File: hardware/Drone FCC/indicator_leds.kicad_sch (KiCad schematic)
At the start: 48 parts, among them Q1101 2N7002, Q1102 2N7002, Q1103 2N7002, Q1104 2N7002, Q1105 2N7002, Q1106 2N7002, Q1107 2N7002, Q1108 2N7002, SW1101 SW Proposito General, SW1102 SW Proposito General

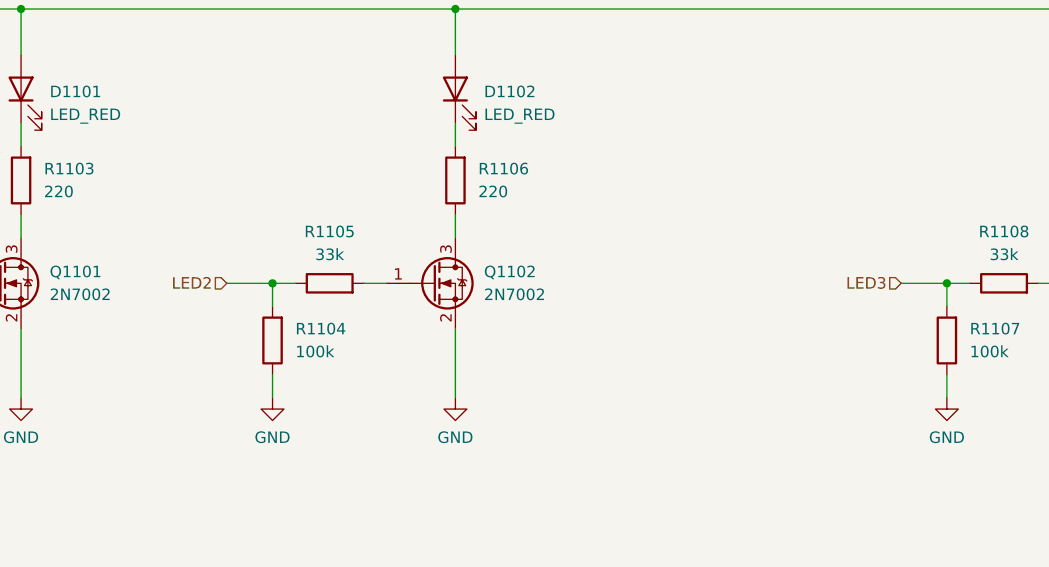
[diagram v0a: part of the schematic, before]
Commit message: re routed everything with newer dimensions
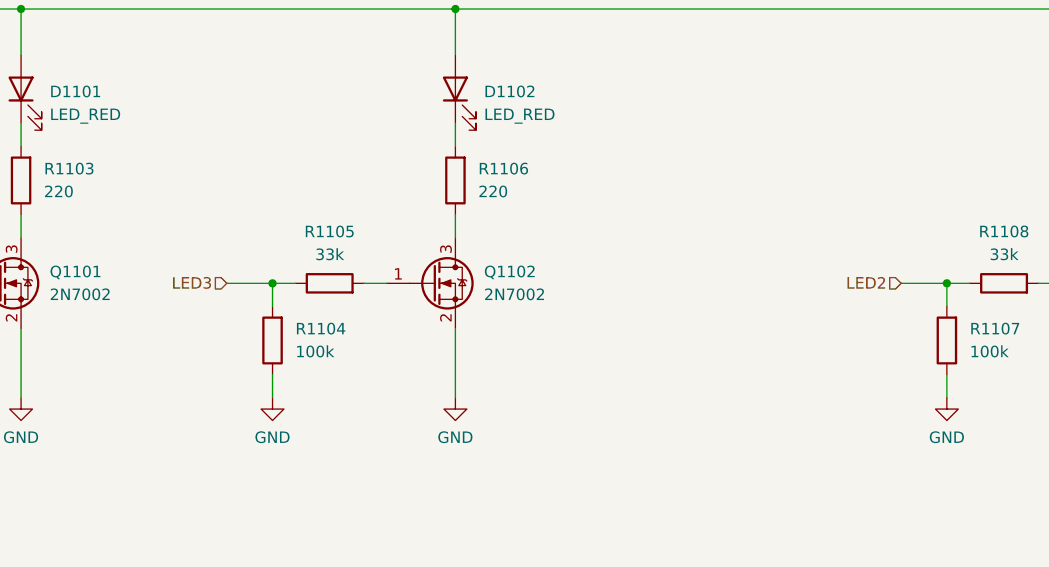
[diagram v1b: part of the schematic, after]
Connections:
- net LED2: now also R1107.2, R1108.1; no longer R1104.2, R1105.1
- net LED3: now also R1104.2, R1105.1; no longer R1107.2, R1108.1
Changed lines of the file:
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@@
     (effects (font (size 1.27 1.27)) (justify right))
   )
-  (hierarchical_label "LED3" (shape input) (at 167.64 47.625 180)
+  (hierarchical_label "LED3" (shape input) (at 92.71 47.625 180)
     (effects (font (size 1.27 1.27)) (justify right))
   )
@@
     (effects (font (size 1.27 1.27)) (justify right))
   )
-  (hierarchical_label "LED2" (shape input) (at 92.71 47.625 180)
+  (hierarchical_label "LED2" (shape input) (at 167.64 47.625 180)
     (effects (font (size 1.27 1.27)) (justify right))
   )

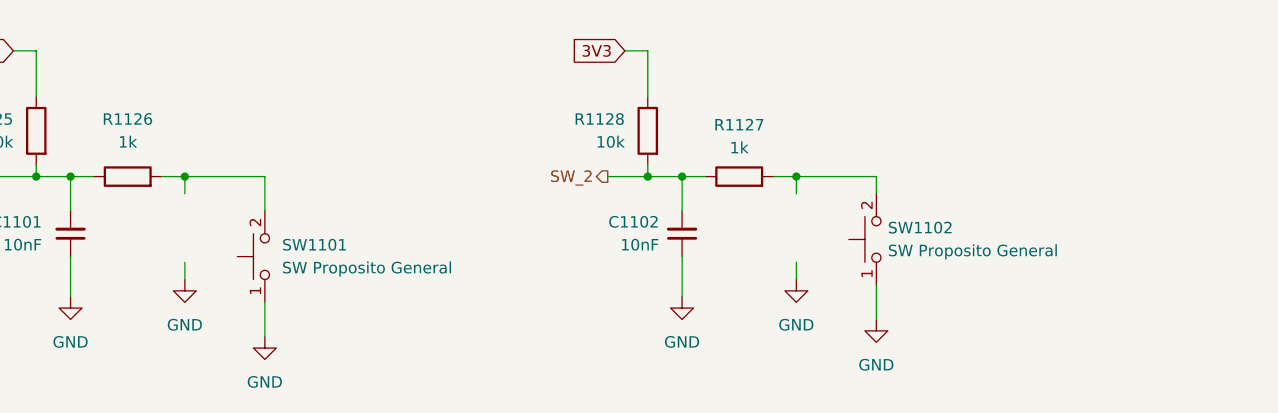
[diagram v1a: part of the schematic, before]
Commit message: tidying up the schematic
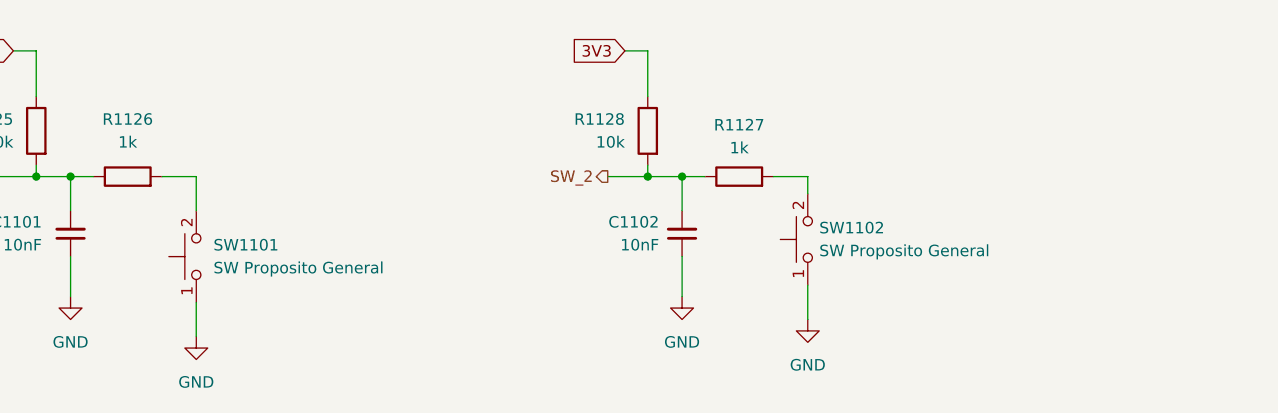
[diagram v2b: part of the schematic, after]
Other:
- moved on the sheet: SW1101, SW1102
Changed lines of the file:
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@@
   (junction (at 29.845 167.64) (diameter 0) (color 0 0 0 0)
   )
-  (junction (at 110.49 167.64) (diameter 0) (color 0 0 0 0)
-  )
   (junction (at 93.98 167.64) (diameter 0) (color 0 0 0 0)
   )
-  (junction (at 42.545 167.64) (diameter 0) (color 0 0 0 0)
-  )
   (junction (at 220.98 47.625) (diameter 0) (color 0 0 0 0)
   )
@@
     (stroke (width 0) (type default) (color 0 0 0 0))
   )
-  (wire (pts (xy 51.435 167.64) (xy 51.435 171.45))
+  (wire (pts (xy 43.815 167.64) (xy 43.815 171.45))
+    (stroke (width 0) (type default) (color 0 0 0 0))
+  )
+  (wire (pts (xy 40.005 167.64) (xy 43.815 167.64))
     (stroke (width 0) (type default) (color 0 0 0 0))
   )
@@
     (stroke (width 0) (type default) (color 0 0 0 0))
   )
-  (wire (pts (xy 119.38 167.64) (xy 119.38 169.545))
+  (wire (pts (xy 111.76 167.64) (xy 111.76 169.545))
     (stroke (width 0) (type default) (color 0 0 0 0))
   )
@@
     (stroke (width 0) (type default) (color 0 0 0 0))
   )
-  (wire (pts (xy 110.49 177.165) (xy 110.49 179.07))
-    (stroke (width 0) (type default) (color 0 0 0 0))
-  )
   (wire (pts (xy 106.045 127.635) (xy 108.585 127.635))
     (stroke (width 0) (type default) (color 0 0 0 0))
@@
     (stroke (width 0) (type default) (color 0 0 0 0))
   )
-  (wire (pts (xy 110.49 167.64) (xy 119.38 167.64))
+  (wire (pts (xy 107.95 167.64) (xy 111.76 167.64))
     (stroke (width 0) (type default) (color 0 0 0 0))
   )
@@
     (stroke (width 0) (type default) (color 0 0 0 0))
   )
-  (wire (pts (xy 40.005 167.64) (xy 42.545 167.64))
-    (stroke (width 0) (type default) (color 0 0 0 0))
-  )
   (wire (pts (xy 116.205 132.715) (xy 116.205 140.335))
     (stroke (width 0) (type default) (color 0 0 0 0))
@@
     (stroke (width 0) (type default) (color 0 0 0 0))
   )
-  (wire (pts (xy 119.38 179.705) (xy 119.38 183.515))
+  (wire (pts (xy 111.76 179.705) (xy 111.76 183.515))
     (stroke (width 0) (type default) (color 0 0 0 0))
   )
@@
     (stroke (width 0) (type default) (color 0 0 0 0))
   )
-  (wire (pts (xy 42.545 177.165) (xy 42.545 179.07))
-    (stroke (width 0) (type default) (color 0 0 0 0))
-  )
   (wire (pts (xy 97.79 176.53) (xy 97.79 180.975))
     (stroke (width 0) (type default) (color 0 0 0 0))
@@
     (stroke (width 0) (type default) (color 0 0 0 0))
   )
-  (wire (pts (xy 51.435 181.61) (xy 51.435 185.42))
+  (wire (pts (xy 43.815 181.61) (xy 43.815 185.42))
     (stroke (width 0) (type default) (color 0 0 0 0))
   )
@@
     (stroke (width 0) (type default) (color 0 0 0 0))
   )
-  (wire (pts (xy 42.545 167.64) (xy 42.545 169.545))
-    (stroke (width 0) (type default) (color 0 0 0 0))
-  )
   (wire (pts (xy 231.14 127.635) (xy 233.68 127.635))
     (stroke (width 0) (type default) (color 0 0 0 0))
@@
     (stroke (width 0) (type default) (color 0 0 0 0))
   )
-  (wire (pts (xy 110.49 167.64) (xy 110.49 169.545))
-    (stroke (width 0) (type default) (color 0 0 0 0))
-  )
   (wire (pts (xy 69.85 40.005) (xy 69.85 42.545))
     (stroke (width 0) (type default) (color 0 0 0 0))
   )
-  (wire (pts (xy 42.545 167.64) (xy 51.435 167.64))
-    (stroke (width 0) (type default) (color 0 0 0 0))
-  )
   (wire (pts (xy 50.165 127.635) (xy 47.625 127.635))
     (stroke (width 0) (type default) (color 0 0 0 0))
@@
   )
   (wire (pts (xy 116.205 97.155) (xy 193.04 97.155))
-    (stroke (width 0) (type default) (color 0 0 0 0))
-  )
-  (wire (pts (xy 107.95 167.64) (xy 110.49 167.64))
     (stroke (width 0) (type default) (color 0 0 0 0))
   )
@@
     (pin "1")
   )
-  (symbol (lib_id "power:GND") (at 119.38 183.515 0) (unit 1)
-    (in_bom yes) (on_board yes) (fields_autoplaced)
-    (property "Reference" "#PWR0165" (id 0) (at 119.38 189.865 0)
-      (effects (font (size 1.27 1.27)) hide)
-    )
-    (property "Value" "GND" (id 1) (at 119.38 188.595 0))
-    (property "Footprint" "" (id 2) (at 119.38 183.515 0)
-      (effects (font (size 1.27 1.27)) hide)
-    )
-    (property "Datasheet" "" (id 3) (at 119.38 183.515 0)
+  (symbol (lib_id "power:GND") (at 111.76 183.515 0) (unit 1)
+    (in_bom yes) (on_board yes) (fields_autoplaced)
+    (property "Reference" "#PWR0165" (id 0) (at 111.76 189.865 0)
+      (effects (font (size 1.27 1.27)) hide)
+    )
+    (property "Value" "GND" (id 1) (at 111.76 188.595 0))
+    (property "Footprint" "" (id 2) (at 111.76 183.515 0)
+      (effects (font (size 1.27 1.27)) hide)
+    )
+    (property "Datasheet" "" (id 3) (at 111.76 183.515 0)
       (effects (font (size 1.27 1.27)) hide)
     )
@@
     (pin "1")
   )
-  (symbol (lib_id "power:GND") (at 42.545 179.07 0) (unit 1)
-    (in_bom yes) (on_board yes) (fields_autoplaced)
-    (property "Reference" "#PWR0215" (id 0) (at 42.545 185.42 0)
-      (effects (font (size 1.27 1.27)) hide)
-    )
-    (property "Value" "GND" (id 1) (at 42.545 184.15 0))
-    (property "Footprint" "" (id 2) (at 42.545 179.07 0)
-      (effects (font (size 1.27 1.27)) hide)
-    )
-    (property "Datasheet" "" (id 3) (at 42.545 179.07 0)
-      (effects (font (size 1.27 1.27)) hide)
-    )
-    (pin "1")
-  )
   (symbol (lib_id "Device:LED") (at 67.945 106.045 90) (unit 1)
     (in_bom yes) (on_board yes) (fields_autoplaced)
@@
     (pin "3")
   )
-  (symbol (lib_id "power:GND") (at 110.49 179.07 0) (unit 1)
-    (in_bom yes) (on_board yes) (fields_autoplaced)
-    (property "Reference" "#PWR0217" (id 0) (at 110.49 185.42 0)
-      (effects (font (size 1.27 1.27)) hide)
-    )
-    (property "Value" "GND" (id 1) (at 110.49 184.15 0))
-    (property "Footprint" "" (id 2) (at 110.49 179.07 0)
-      (effects (font (size 1.27 1.27)) hide)
-    )
-    (property "Datasheet" "" (id 3) (at 110.49 179.07 0)
-      (effects (font (size 1.27 1.27)) hide)
-    )
-    (pin "1")
-  )
   (symbol (lib_id "Device:R") (at 220.98 133.985 180) (unit 1)
     (in_bom yes) (on_board yes) (fields_autoplaced)
@@
     (pin "2")
   )
-  (symbol (lib_id "434121043816:SW_SPST") (at 119.38 174.625 90) (unit 1)
+  (symbol (lib_id "434121043816:SW_SPST") (at 111.76 174.625 90) (unit 1)
     (in_bom yes) (on_board yes)
-    (property "Reference" "SW1102" (id 0) (at 120.65 173.3549 90)
-      (effects (font (size 1.27 1.27)) (justify right))
-    )
-    (property "Value" "SW Proposito General" (id 1) (at 120.65 175.8949 90)
-      (effects (font (size 1.27 1.27)) (justify right))
-    )
-    (property "Footprint" "434121043816:434121043816" (id 2) (at 119.38 174.625 0)
-      (effects (font (size 1.27 1.27)) hide)
-    )
-    (property "Datasheet" "~" (id 3) (at 119.38 174.625 0)
+    (property "Reference" "SW1102" (id 0) (at 113.03 173.3549 90)
+      (effects (font (size 1.27 1.27)) (justify right))
+    )
+    (property "Value" "SW Proposito General" (id 1) (at 113.03 175.8949 90)
+      (effects (font (size 1.27 1.27)) (justify right))
+    )
+    (property "Footprint" "434121043816:434121043816" (id 2) (at 111.76 174.625 0)
+      (effects (font (size 1.27 1.27)) hide)
+    )
+    (property "Datasheet" "~" (id 3) (at 111.76 174.625 0)
       (effects (font (size 1.27 1.27)) hide)
     )
@@
     (pin "1")
   )
-  (symbol (lib_id "434121043816:SW_SPST") (at 51.435 176.53 90) (unit 1)
-    (in_bom yes) (on_board yes) (fields_autoplaced)
-    (property "Reference" "SW1101" (id 0) (at 53.34 175.2599 90)
-      (effects (font (size 1.27 1.27)) (justify right))
-    )
-    (property "Value" "SW Proposito General" (id 1) (at 53.34 177.7999 90)
-      (effects (font (size 1.27 1.27)) (justify right))
-    )
-    (property "Footprint" "434121043816:434121043816" (id 2) (at 51.435 176.53 0)
-      (effects (font (size 1.27 1.27)) hide)
-    )
-    (property "Datasheet" "~" (id 3) (at 51.435 176.53 0)
+  (symbol (lib_id "434121043816:SW_SPST") (at 43.815 176.53 90) (unit 1)
+    (in_bom yes) (on_board yes) (fields_autoplaced)
+    (property "Reference" "SW1101" (id 0) (at 45.72 175.2599 90)
+      (effects (font (size 1.27 1.27)) (justify right))
+    )
+    (property "Value" "SW Proposito General" (id 1) (at 45.72 177.7999 90)
+      (effects (font (size 1.27 1.27)) (justify right))
+    )
+    (property "Footprint" "434121043816:434121043816" (id 2) (at 43.815 176.53 0)
+      (effects (font (size 1.27 1.27)) hide)
+    )
+    (property "Datasheet" "~" (id 3) (at 43.815 176.53 0)
       (effects (font (size 1.27 1.27)) hide)
     )
@@
     (pin "1")
   )
-  (symbol (lib_id "power:GND") (at 51.435 185.42 0) (unit 1)
-    (in_bom yes) (on_board yes) (fields_autoplaced)
-    (property "Reference" "#PWR0214" (id 0) (at 51.435 191.77 0)
-      (effects (font (size 1.27 1.27)) hide)
-    )
-    (property "Value" "GND" (id 1) (at 51.435 190.5 0))
-    (property "Footprint" "" (id 2) (at 51.435 185.42 0)
-      (effects (font (size 1.27 1.27)) hide)
-    )
-    (property "Datasheet" "" (id 3) (at 51.435 185.42 0)
-      (effects (font (size 1.27 1.27)) hide)
-    )
+  (symbol (lib_id "power:GND") (at 43.815 185.42 0) (unit 1)
+    (in_bom yes) (on_board yes) (fields_autoplaced)
+    (property "Reference" "#PWR0214" (id 0) (at 43.815 191.77 0)
+      (effects (font (size 1.27 1.27)) hide)
+    )
+    (property "Value" "GND" (id 1) (at 43.815 190.5 0))
+    (property "Footprint" "" (id 2) (at 43.815 185.42 0)
+      (effects (font (size 1.27 1.27)) hide)
+    )
+    (property "Datasheet" "" (id 3) (at 43.815 185.42 0)
+      (effects (font (size 1.27 1.27)) hide)
+    )

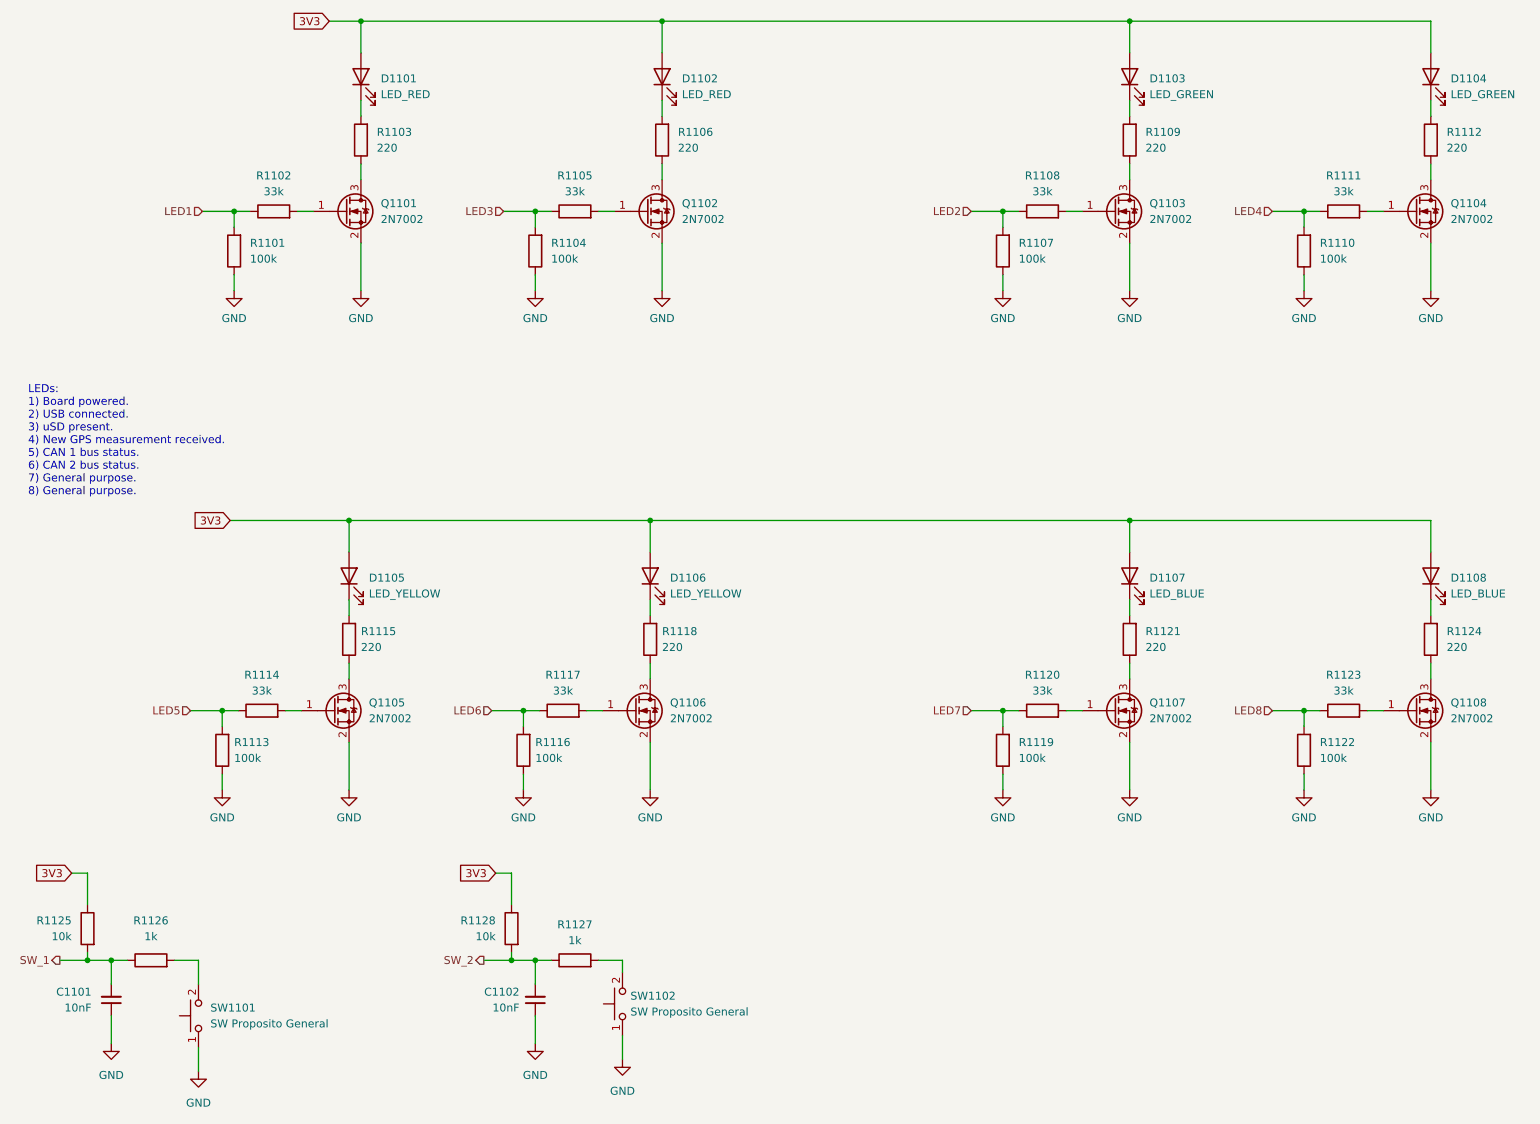
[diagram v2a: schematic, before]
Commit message: re enumeation of componentes
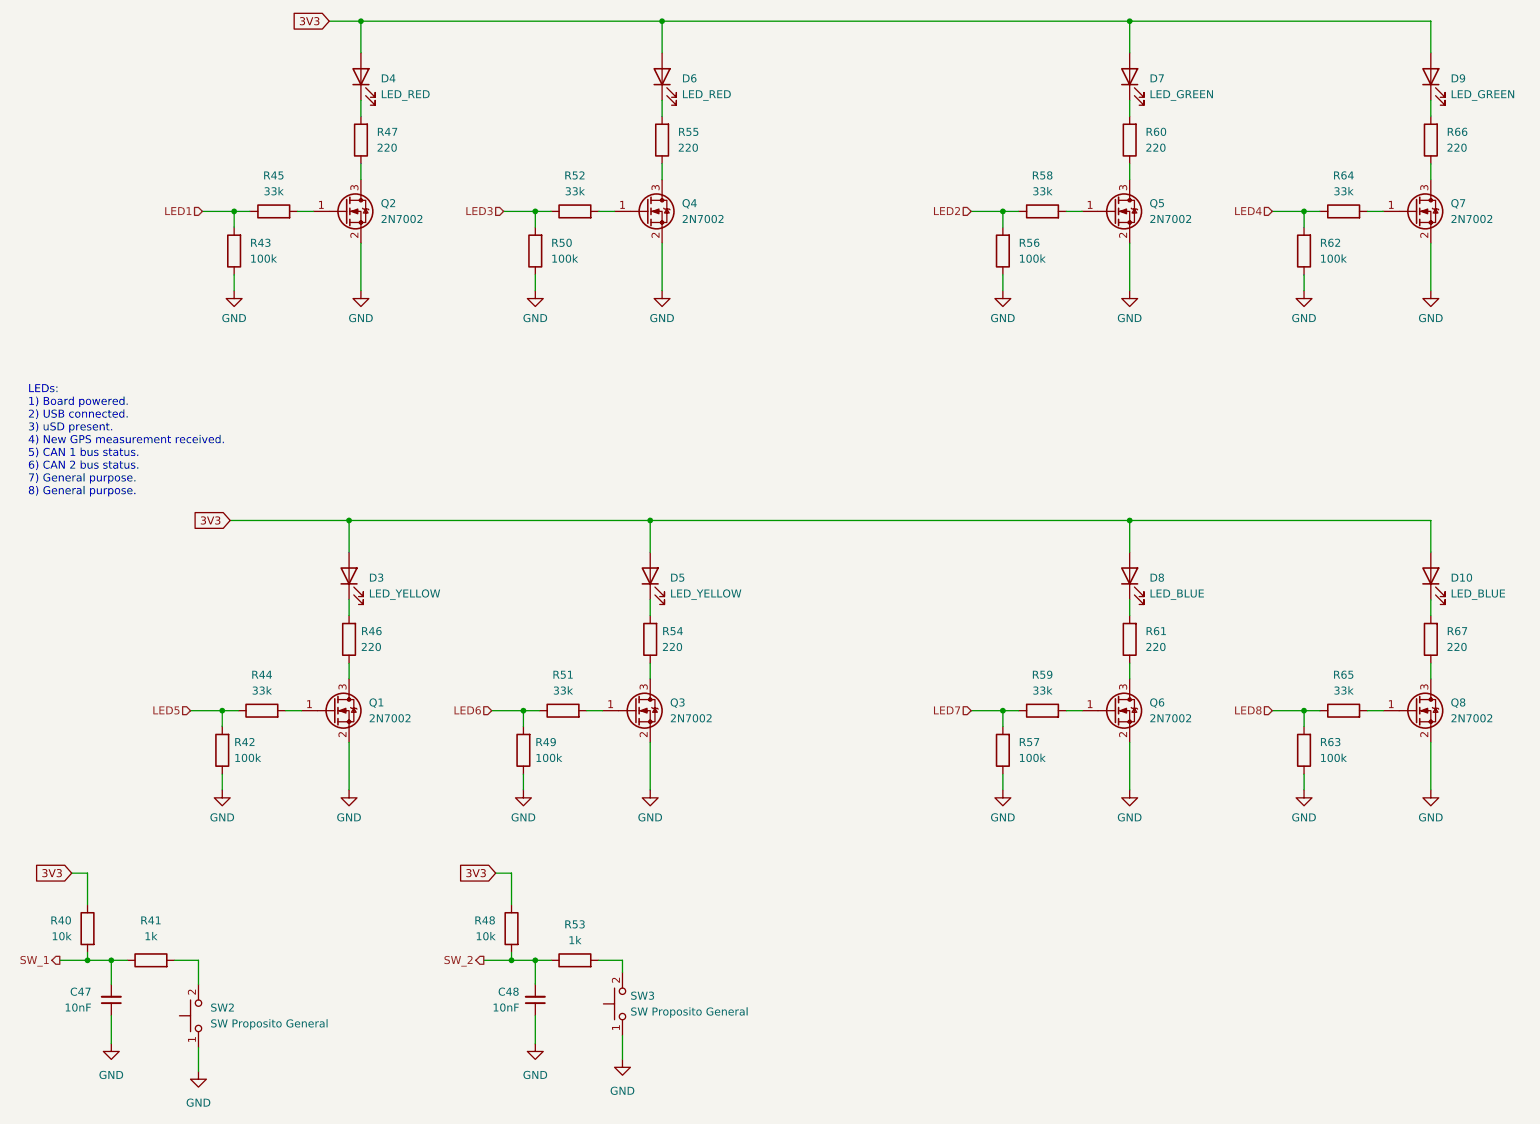
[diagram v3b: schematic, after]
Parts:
- renumbered C1101 to C47, C1102 to C48, D1108 to D10, D1105 to D3, D1101 to D4, D1106 to D5, D1102 to D6, D1103 to D7, D1107 to D8, D1104 to D9, Q1105 to Q1, Q1101 to Q2, Q1106 to Q3, Q1102 to Q4, Q1103 to Q5, Q1107 to Q6, Q1104 to Q7, Q1108 to Q8, R1125 to R40, R1126 to R41, R1113 to R42, R1101 to R43, R1114 to R44, R1102 to R45, R1115 to R46, R1103 to R47, R1128 to R48, R1116 to R49, R1104 to R50, R1117 to R51, R1105 to R52, R1127 to R53, R1118 to R54, R1106 to R55, R1107 to R56, R1119 to R57, R1108 to R58, R1120 to R59, R1109 to R60, R1121 to R61, R1110 to R62, R1122 to R63, R1111 to R64, R1123 to R65, R1112 to R66, R1124 to R67, SW1101 to SW2, SW1102 to SW3
